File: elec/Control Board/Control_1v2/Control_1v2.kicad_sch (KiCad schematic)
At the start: 168 parts, among them J1 DB9_Female_MountingHoles, J10 Conn_02x12_Odd_Even, J11 Con_01x02_2.5mm, J14 Conn_01x10, J2 Conn_01x08, J25 Con_01x02_2.5mm, J26 Conn_01x10, J27 Conn_02x12_Odd_Even, J28 Con_01x02_2.5mm, J29 Conn_01x10, J3 Conn_01x08, J37 Conn_01x04, J4 Conn_01x08, J5 Conn_01x08, J6 Conn_01x08, J7 Conn_01x10, J8 Conn_02x18_Odd_Even, J9 Conn_01x10, Q601 BSS138

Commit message: PCB V1.2. Update with footprint JST_PUD_B24B-PUDSS_2x12_P2.00mm_Vertical.
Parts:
- J10, J27: footprint PubInv_KiCad_PCB.pretty:PinHeader_2x12_P2.00mm_Vertical_JST -> Connector_JST:JST_PUD_B24B-PUDSS_2x12_P2.00mm_Vertical
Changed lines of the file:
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@@
       (effects (font (size 1.27 1.27)))
     )
-    (property "Footprint" "PubInv_KiCad_PCB.pretty:PinHeader_2x12_P2.00mm_Vertical_JST" (at 450.85 53.34 0)
+    (property "Footprint" "Connector_JST:JST_PUD_B24B-PUDSS_2x12_P2.00mm_Vertical" (at 450.85 53.34 0)
       (effects (font (size 1.27 1.27)) hide)
     )
@@
       (effects (font (size 1.27 1.27)))
     )
-    (property "Footprint" "PubInv_KiCad_PCB.pretty:PinHeader_2x12_P2.00mm_Vertical_JST" (at 450.85 124.46 0)
-      (effects (font (size 1.27 1.27)) hide)
-    )
+    (property "Footprint" "Connector_JST:JST_PUD_B24B-PUDSS_2x12_P2.00mm_Vertical" (at 450.85 124.46 0)
+      (effects (font (size 1.27 1.27)) hide)
+    )

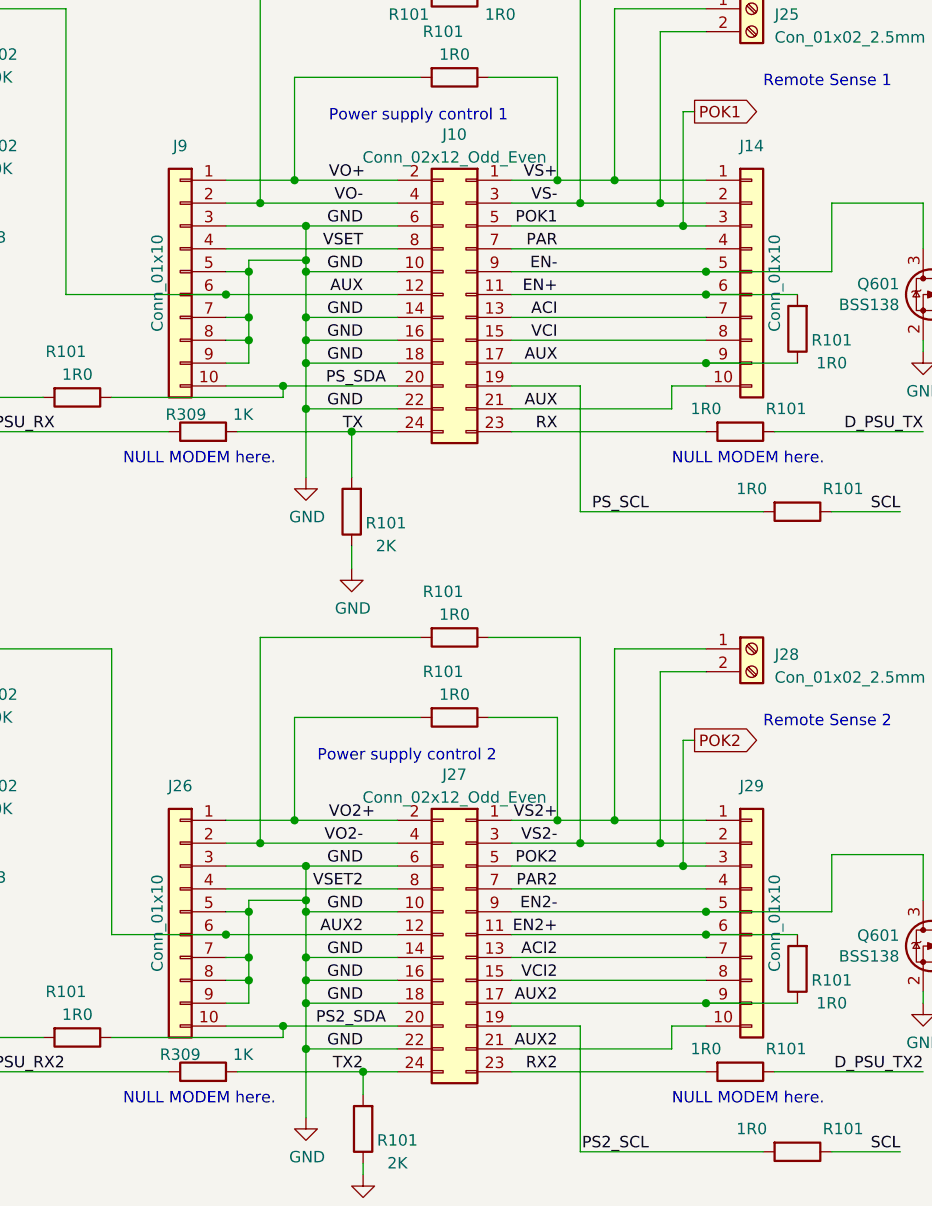
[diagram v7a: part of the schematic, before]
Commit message: PCB V1.2. Update with footprint JST_PUD_B24B-PUDSS_2x12_P2.00mm_Vertical with STEP file.
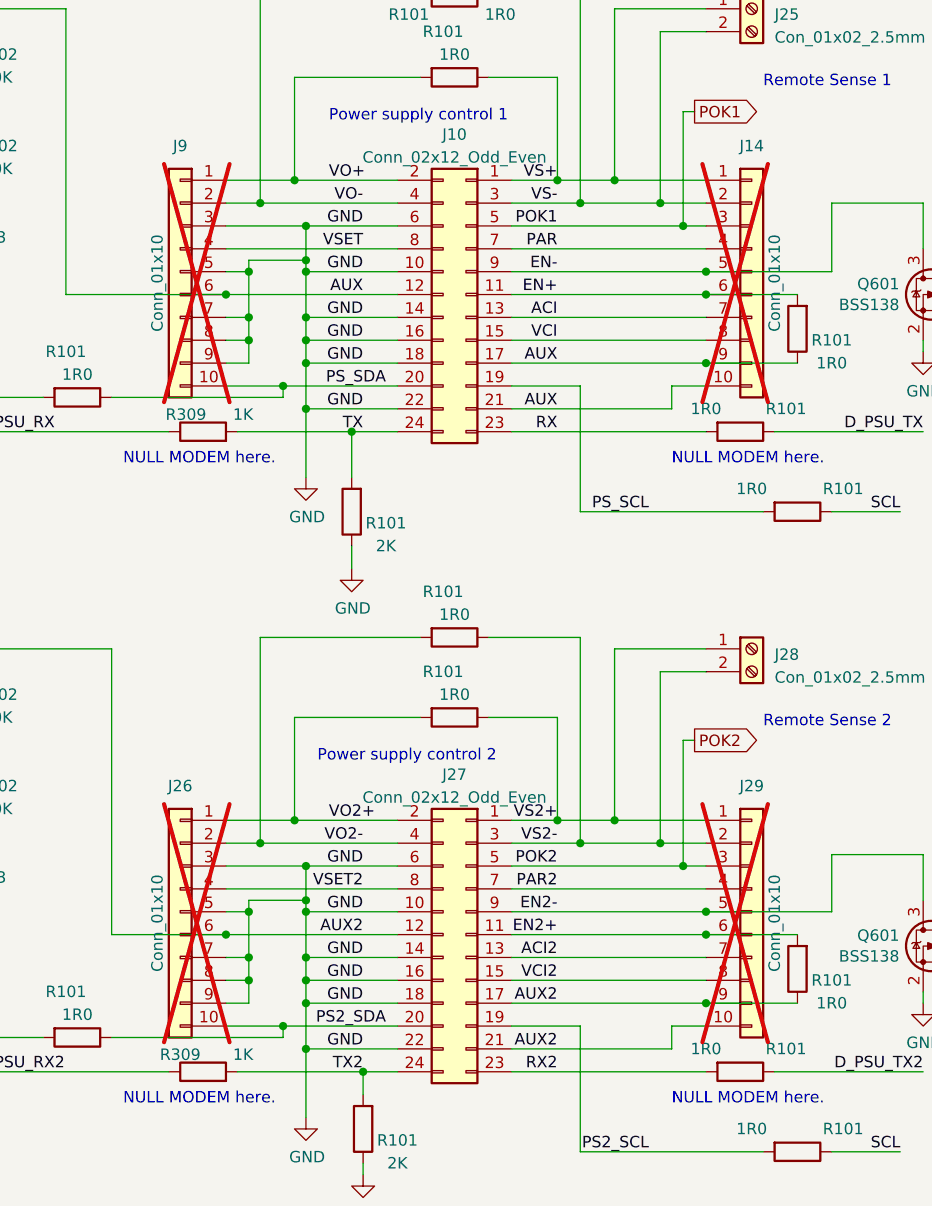
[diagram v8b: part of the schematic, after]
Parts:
- J10, J27: footprint Connector_JST:JST_PUD_B24B-PUDSS_2x12_P2.00mm_Vertical -> PubInv_KiCad_PCB:JST_PHD_B24B-PHDSS_2x12_P2.00mm_Vertical
- J14, J26, J29, J9: now not fitted
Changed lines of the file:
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@@
   )
   (symbol (lib_id "Connector_Generic:Conn_01x10") (at 419.1 50.8 0) (mirror y) (unit 1)
-    (in_bom yes) (on_board yes) (dnp no)
+    (in_bom yes) (on_board yes) (dnp yes)
     (property "Reference" "J9" (at 419.1 36.83 0)
       (effects (font (size 1.27 1.27)))
@@
     (pin "DAC0")
     (pin "DAC1")
-    (pin "ND")
     (pin "GND1")
     (pin "GND2")
@@
     (pin "MISO")
     (pin "MOSI")
+    (pin "ND")
     (pin "RST1")
     (pin "RST2")
@@
   )
   (symbol (lib_id "Connector_Generic:Conn_01x10") (at 482.6 121.92 0) (unit 1)
-    (in_bom yes) (on_board yes) (dnp no)
+    (in_bom yes) (on_board yes) (dnp yes)
     (property "Reference" "J29" (at 482.6 107.95 0)
       (effects (font (size 1.27 1.27)))
@@
       (effects (font (size 1.27 1.27)))
     )
-    (property "Footprint" "Connector_JST:JST_PUD_B24B-PUDSS_2x12_P2.00mm_Vertical" (at 450.85 53.34 0)
+    (property "Footprint" "PubInv_KiCad_PCB:JST_PHD_B24B-PHDSS_2x12_P2.00mm_Vertical" (at 450.85 53.34 0)
       (effects (font (size 1.27 1.27)) hide)
     )
@@
   )
   (symbol (lib_id "Connector_Generic:Conn_01x10") (at 482.6 50.8 0) (unit 1)
-    (in_bom yes) (on_board yes) (dnp no)
+    (in_bom yes) (on_board yes) (dnp yes)
     (property "Reference" "J14" (at 482.6 36.83 0)
       (effects (font (size 1.27 1.27)))
@@
       (effects (font (size 1.27 1.27)))
     )
-    (property "Footprint" "Connector_JST:JST_PUD_B24B-PUDSS_2x12_P2.00mm_Vertical" (at 450.85 124.46 0)
+    (property "Footprint" "PubInv_KiCad_PCB:JST_PHD_B24B-PHDSS_2x12_P2.00mm_Vertical" (at 450.85 124.46 0)
       (effects (font (size 1.27 1.27)) hide)
     )
@@
   )
   (symbol (lib_id "Connector_Generic:Conn_01x10") (at 419.1 121.92 0) (mirror y) (unit 1)
-    (in_bom yes) (on_board yes) (dnp no)
+    (in_bom yes) (on_board yes) (dnp yes)
     (property "Reference" "J26" (at 419.1 107.95 0)
       (effects (font (size 1.27 1.27)))
